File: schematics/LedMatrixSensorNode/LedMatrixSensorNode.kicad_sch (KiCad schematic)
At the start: 11 parts, among them J2 BH1750, J3 SCD41, J4 HTU21D, J5 HLK-LD2450, J6 HLK-LD2410, J7 Beeper, J9 LED Matrrix, U1 XIAO-ESP32-S3-Plus-SMD, U2 DC/DC

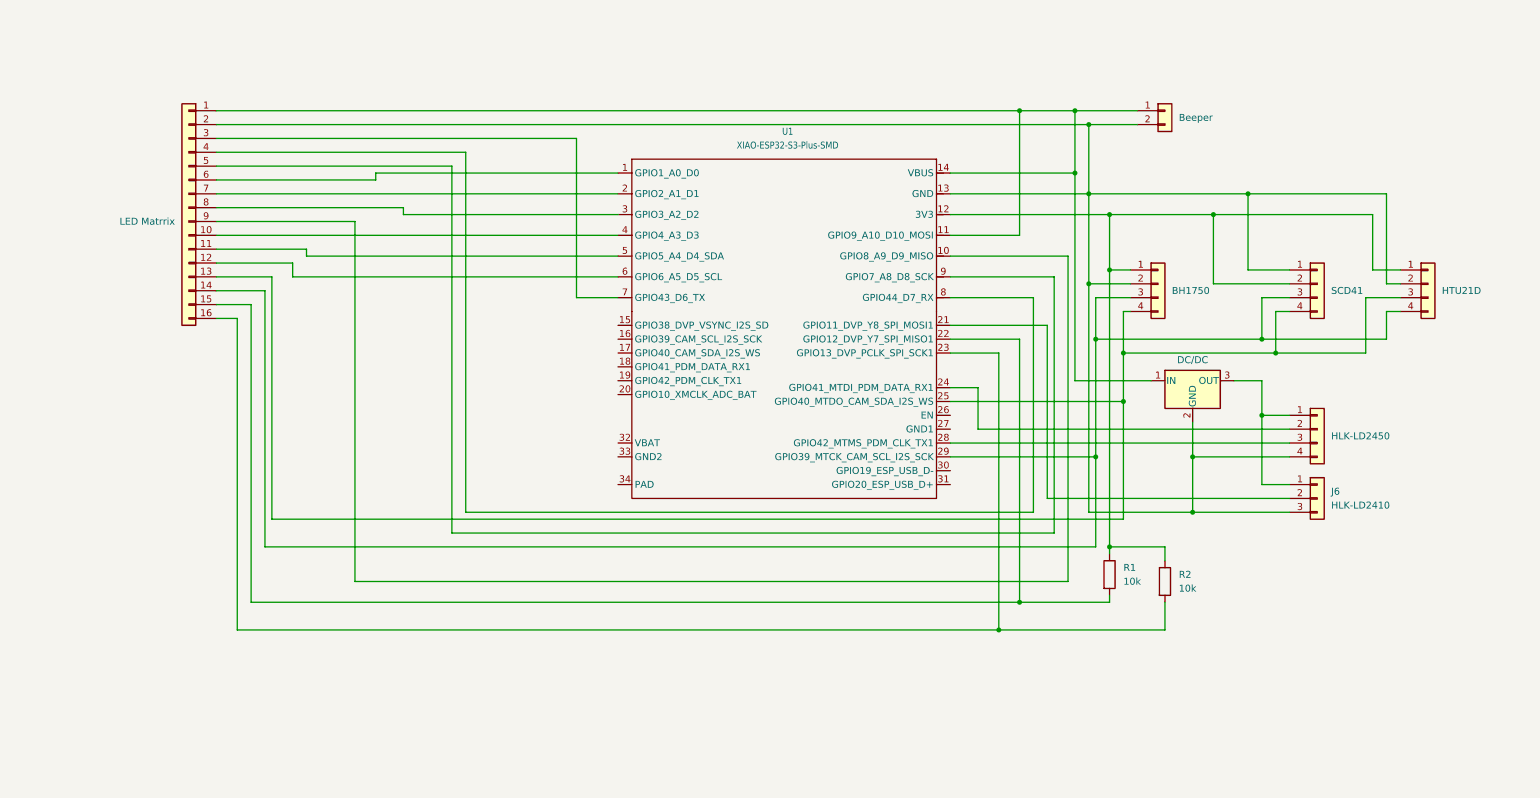
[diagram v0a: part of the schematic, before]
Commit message: Added WI-Fi config, OTA, CO2, temperature, humidity sensors, MQTT for sensors
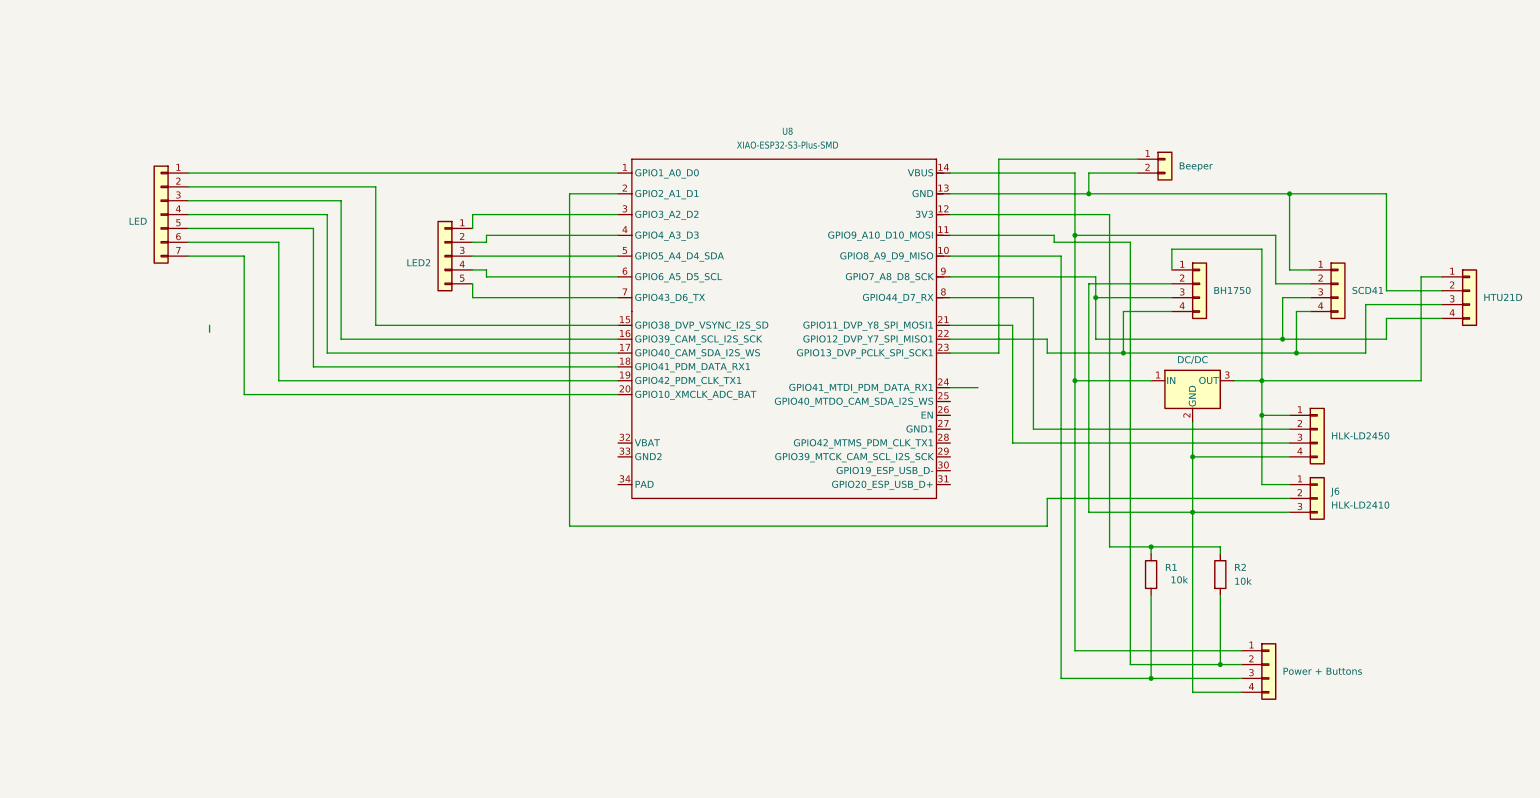
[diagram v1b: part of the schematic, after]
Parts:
- removed J9: LED Matrrix, symbol Connector_Generic:Conn_01x16
- removed U1: XIAO-ESP32-S3-Plus-SMD, Seeed_Studio_XIAO_Series:XIAO-ESP32-S3-Plus-SMD, symbol Seeed_Studio_XIAO_Series:XIAO-ESP32-S3 Plus-SMD
- added J10: LED2, symbol Connector_Generic:Conn_01x05
- added J8: Power + Buttons, symbol Connector_Generic:Conn_01x04
- added J9: LED, symbol Connector_Generic:Conn_01x07
- added U8: XIAO-ESP32-S3-Plus-SMD, Seeed_Studio_XIAO_Series:XIAO-ESP32-S3-Plus-SMD, symbol Seeed_Studio_XIAO_Series:XIAO-ESP32-S3 Plus-SMD
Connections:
- net at U2.1 (IN): now also J3.2 (Pin_2), J8.1 (Pin_1), U8.14 (VBUS); no longer J7.1 (Pin_1)
- net at J2.2 (Pin_2), J5.4 (Pin_4), J6.3 (Pin_3)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: now also J8.4 (Pin_4); no longer J3.1 (Pin_1), J4.2 (Pin_2), J7.2 (Pin_2)
- net at J6.2 (Pin_2): now also U8.2 (GPIO2_A1_D1)
- net at R1.2: now also J8.3 (Pin_3), U8.10 (GPIO8_A9_D9_MISO)
- net at R2.2: now also J8.2 (Pin_2), U8.11 (GPIO9_A10_D10_MOSI)
- net at J5.2 (Pin_2): now also U8.8 (GPIO44_D7_RX)
- net at J2.4 (Pin_4), J3.4 (Pin_4), J4.3 (Pin_3): now also U8.22 (GPIO12_DVP_Y7_SPI_MISO1)
- net at J5.3 (Pin_3): now also U8.21 (GPIO11_DVP_Y8_SPI_MOSI1)
- net at J2.3 (Pin_3), J3.3 (Pin_3), J4.4 (Pin_4): now also U8.9 (GPIO7_A8_D8_SCK)
- net at J5.1 (Pin_1), J6.1 (Pin_1), U2.3 (OUT): now also J2.1 (Pin_1), J4.1 (Pin_1)
- new net: J10.1 (Pin_1), U8.3 (GPIO3_A2_D2)
- new net: J10.2 (Pin_2), U8.4 (GPIO4_A3_D3)
- new net: J10.3 (Pin_3), U8.5 (GPIO5_A4_D4_SDA)
- new net: J10.4 (Pin_4), U8.6 (GPIO6_A5_D5_SCL)
- new net: J10.5 (Pin_5), U8.7 (GPIO43_D6_TX)
- new net: J3.1 (Pin_1), J4.2 (Pin_2), J7.2 (Pin_2), U8.13 (GND)
- new net: R1.1, R2.1, U8.12 (3V3)
- new net: J9.1 (Pin_1), U8.1 (GPIO1_A0_D0)
- new net: J9.2 (Pin_2), U8.15 (GPIO38_DVP_VSYNC_I2S_SD)
- new net: J9.3 (Pin_3), U8.16 (GPIO39_CAM_SCL_I2S_SCK)
- new net: J9.4 (Pin_4), U8.17 (GPIO40_CAM_SDA_I2S_WS)
- new net: J9.5 (Pin_5), U8.18 (GPIO41_PDM_DATA_RX1)
- new net: J9.6 (Pin_6), U8.19 (GPIO42_PDM_CLK_TX1)
- new net: J9.7 (Pin_7), U8.20 (GPIO10_XMCLK_ADC_BAT)
- new net: J7.1 (Pin_1), U8.23 (GPIO13_DVP_PCLK_SPI_SCK1)
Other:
- moved on the sheet: R1, R2

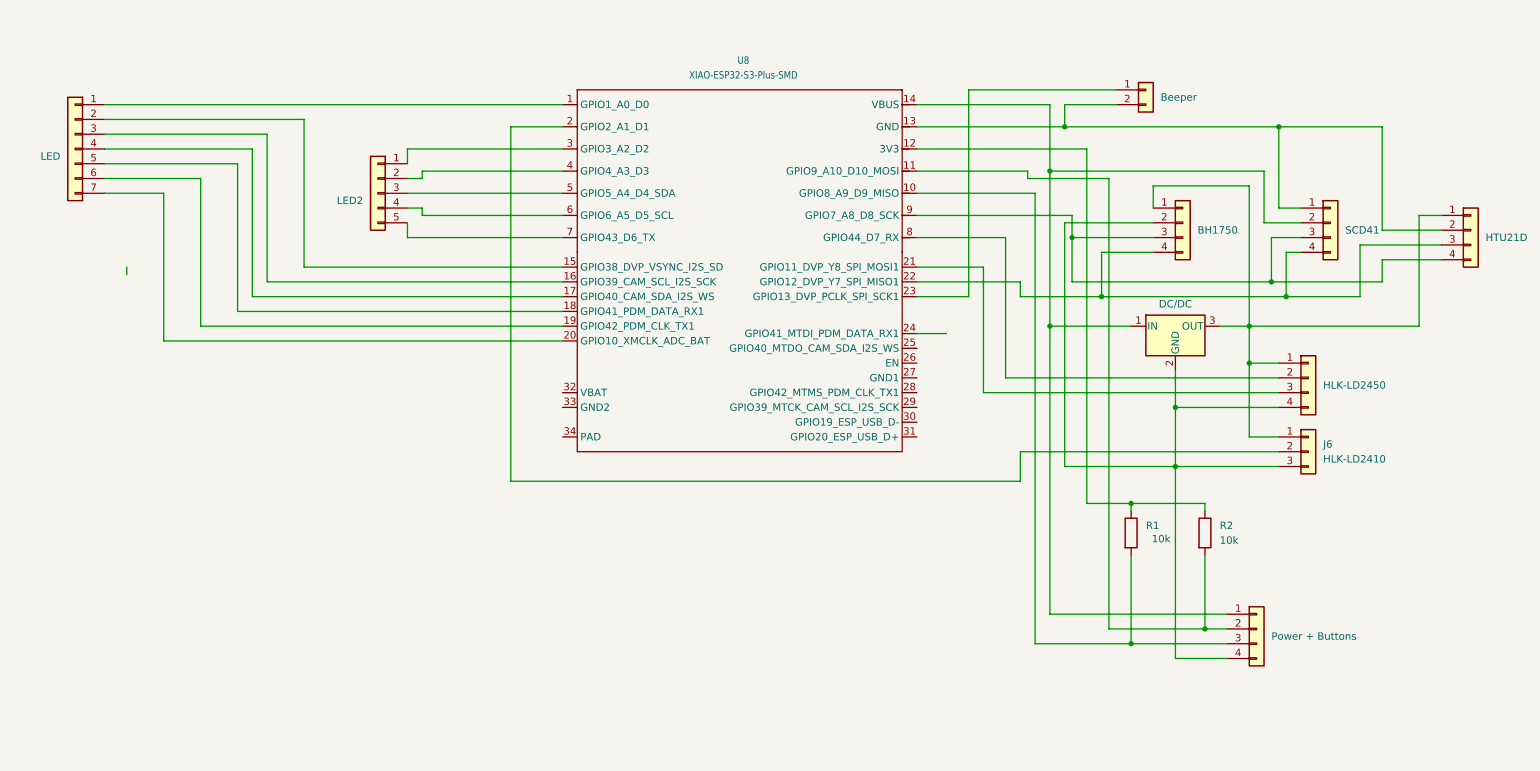
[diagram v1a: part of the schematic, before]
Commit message: Added MQTT mode, message, beeper, LED clock, temp, CO2, message, auto LED brightness, mode / LED off buttons
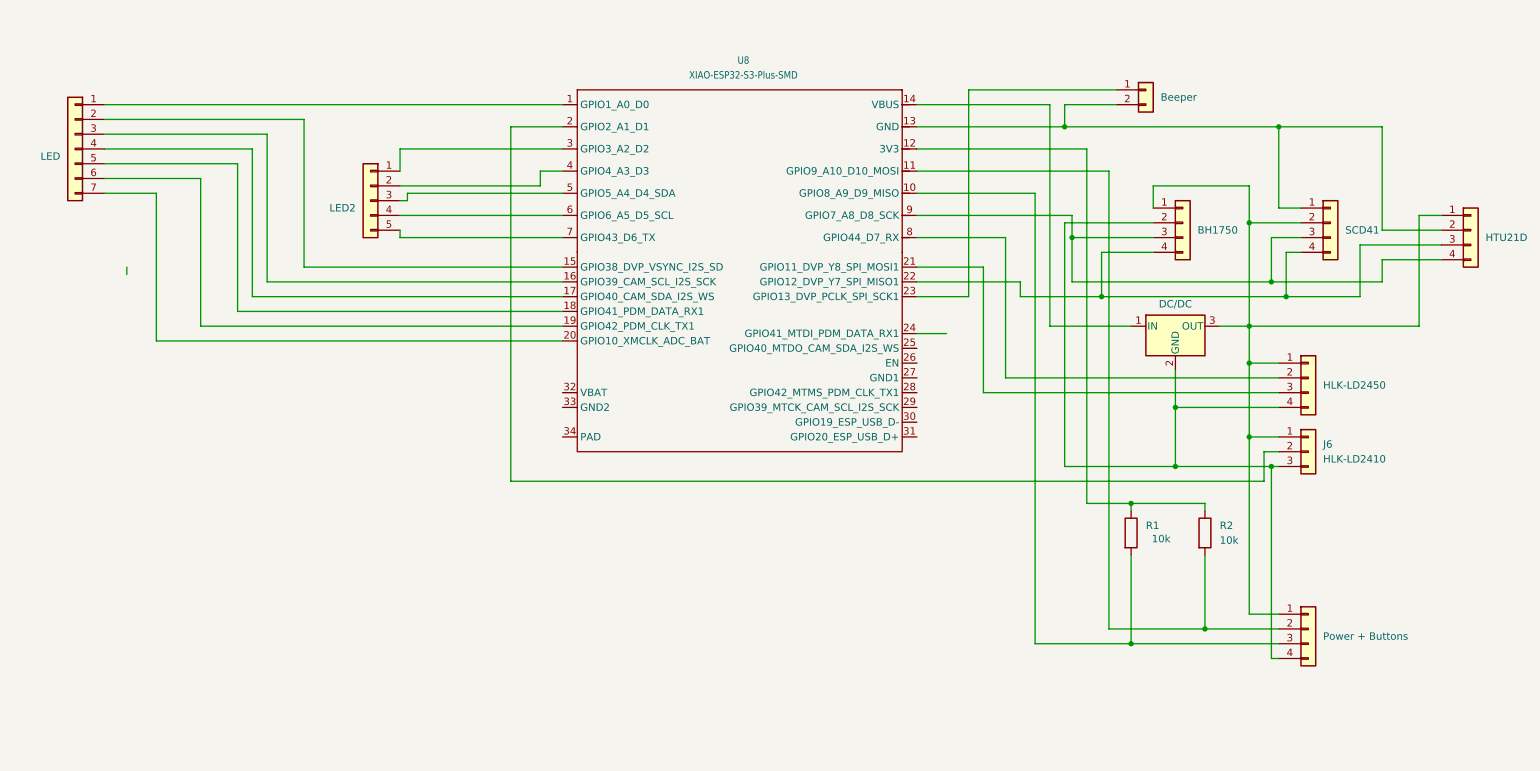
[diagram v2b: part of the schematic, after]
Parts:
- removed J10: LED2, symbol Connector_Generic:Conn_01x05
- added J1: LED2, symbol Connector_Generic:Conn_01x05
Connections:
- net at U8.3 (GPIO3_A2_D2): now also J1.1 (Pin_1)
- net at U8.4 (GPIO4_A3_D3): now also J1.2 (Pin_2)
- net at U8.5 (GPIO5_A4_D4_SDA): now also J1.3 (Pin_3)
- net at U8.6 (GPIO6_A5_D5_SCL): now also J1.4 (Pin_4)
- net at U8.7 (GPIO43_D6_TX): now also J1.5 (Pin_5)
- net at J2.1 (Pin_1), J4.1 (Pin_1), J5.1 (Pin_1)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: now also J3.2 (Pin_2), J8.1 (Pin_1)
- net at U2.1 (IN), U8.14 (VBUS): no longer J3.2 (Pin_2), J8.1 (Pin_1)
